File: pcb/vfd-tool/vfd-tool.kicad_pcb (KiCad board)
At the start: 4 copper layers, 95 x 50 mm, 177 parts, among them J1 Conn_ARM_SWD_TagConnect_TC203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, J2 USB_C_Receptacle_USB2.0, J3 Micro_SD_Card, J4 Conn_01x10, J5 Raspberry_Pi_2_3, J6 Conn_02x15_Odd_Even, J7 Conn_02x15_Odd_Even, J8 Conn_02x08_Odd_Even, J9 Conn_01x02_Socket, SW1 SW_Push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

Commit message: pre-final commit
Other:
- board text added: "Pi Zero"
- board text added: "RTC battery"
- board text added: "uSD"
- board text removed: "PCB3D_BR_MCU"
- board text removed: "PCB3D_TL_MCU"
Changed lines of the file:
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@@
 			(layer "F.SilkS"
 				(type "Top Silk Screen")
+				(color "White")
 			)
 			(layer "F.Paste"
@@
 			(layer "F.Mask"
 				(type "Top Solder Mask")
+				(color "Green")
 				(thickness 0.01)
 			)
@@
 			(layer "dielectric 1"
 				(type "prepreg")
-				(color "#808080FF")
+				(color "FR4 natural")
 				(thickness 0.1)
 				(material "FR4")
@@
 			(layer "dielectric 2"
 				(type "core")
+				(color "FR4 natural")
 				(thickness 1.24)
 				(material "FR4")
@@
 			(layer "dielectric 3"
 				(type "prepreg")
+				(color "FR4 natural")
 				(thickness 0.1)
 				(material "FR4")
@@
 			(layer "B.Mask"
 				(type "Bottom Solder Mask")
+				(color "Green")
 				(thickness 0.01)
 			)
@@
 			(layer "B.SilkS"
 				(type "Bottom Silk Screen")
+				(color "White")
 			)
-			(copper_finish "None")
+			(copper_finish "ENIG")
 			(dielectric_constraints no)
 		)
@@
 		)
 	)
+	(gr_rect
+		(start 232.625 93.325)
+		(end 235.6 94.925)
+		(stroke
+			(width 0.1)
+			(type default)
+		)
+		(fill none)
+		(layer "B.SilkS")
+	)
+	(gr_rect
+		(start 214.3 73.975)
+		(end 235.6 94.925)
+		(stroke
+			(width 0.2)
+			(type default)
+		)
+		(fill none)
+		(layer "B.SilkS")
+	)
 	(gr_poly
 		(pts
@@
 		)
 	)
+	(gr_text "RTC battery"
+		(at 163.4 113.475 0)
+		(layer "B.SilkS")
+		(effects
+			(font
+				(size 0.75 0.75)
+				(thickness 0.15)
+				(bold yes)
+			)
+			(justify left bottom mirror)
+		)
+	)
 	(gr_text "JLCJLCJLCJLC"
 		(at 193.1 122.075 0)
@@
 		)
 	)
+	(gr_text "Pi Zero"
+		(at 179.125 88.45 0)
+		(layer "B.SilkS")
+		(effects
+			(font
+				(size 0.75 0.75)
+				(thickness 0.15)
+				(bold yes)
+			)
+			(justify left bottom mirror)
+		)
+	)
+	(gr_text "uSD"
+		(at 235.35 94.65 -0)
+		(layer "B.SilkS")
+		(effects
+			(font
+				(size 0.75 0.75)
+				(thickness 0.15)
+				(bold yes)
+			)
+			(justify left bottom mirror)
+		)
+	)
 	(gr_text "MCU"
 		(at 218.35 89.25 0)
@@
 			)
 			(justify left bottom)
-		)
-	)
-	(gr_text "PCB3D_BR_MCU"
-		(at 237.775 125.925 0)
-		(layer "User.1")
-		(effects
-			(font
-				(size 1 1)
-				(thickness 0.15)
-			)
-			(justify left bottom)
-		)
-	)
-	(gr_text "PCB3D_TL_MCU"
-		(at 129.55 71.975 0)
-		(layer "User.1")
-		(effects
-			(font
-				(size 1 1)
-				(thickness 0.15)
-			)
-			(justify left bottom)

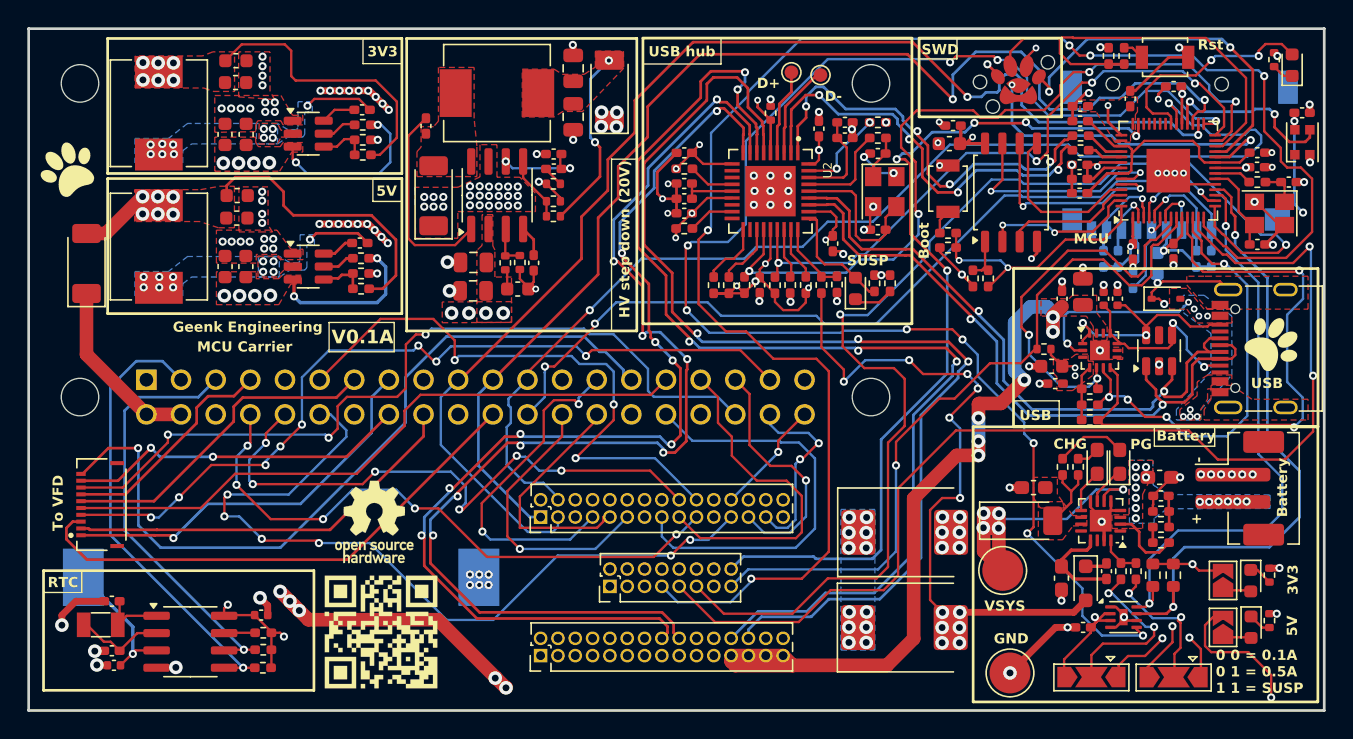
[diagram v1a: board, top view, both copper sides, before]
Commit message: pcb fix for #1 and #2
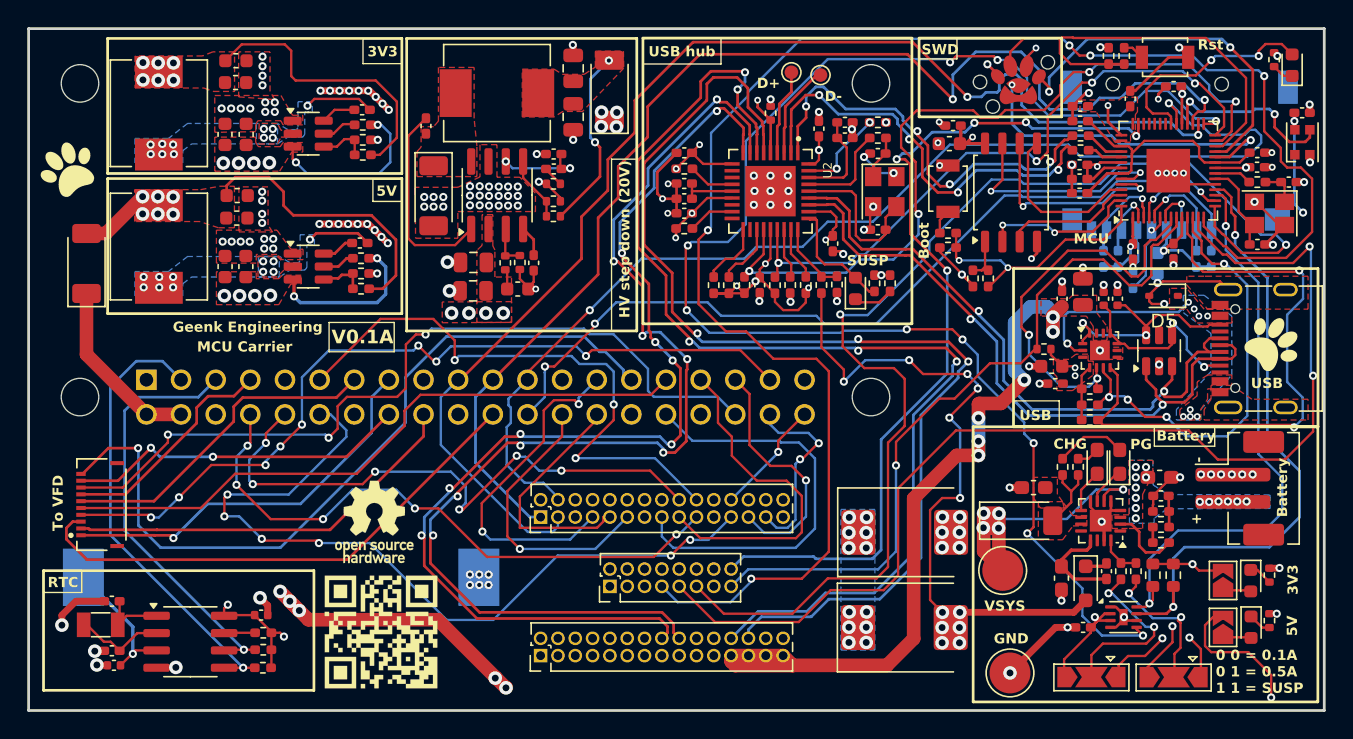
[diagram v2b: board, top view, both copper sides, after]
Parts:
- D11: value LED -> Blue
- D12, D15, D3: value LED -> Green
- D4: value LED -> Purple
- Y3: value 32.768kHz -> 32.768kHz
- moved D5 0.28 mm to (224.9, 93.0), turned to 180 degrees
- turned D10 to -90 degrees
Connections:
- C46 pad 1: Net-(D10-A) -> Net-(D10-K)
- D10 pad 1: GND -> Net-(D10-K)
- D10 pad 2: Net-(D10-A) -> GND
- D5 pad 1: GND -> VBUS
- D5 pad 2: VBUS -> GND
- L3 pad 1: Net-(D10-A) -> Net-(D10-K)
- U10 pad 8: Net-(D10-A) -> Net-(D10-K)
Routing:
- added copper zone on F.Cu, net Net-(D10-K)
- removed copper zone on F.Cu, net Net-(D10-A)
